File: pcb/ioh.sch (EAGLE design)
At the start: 11 parts, among them Q1 MOSFET-NCHANNEL2N7000

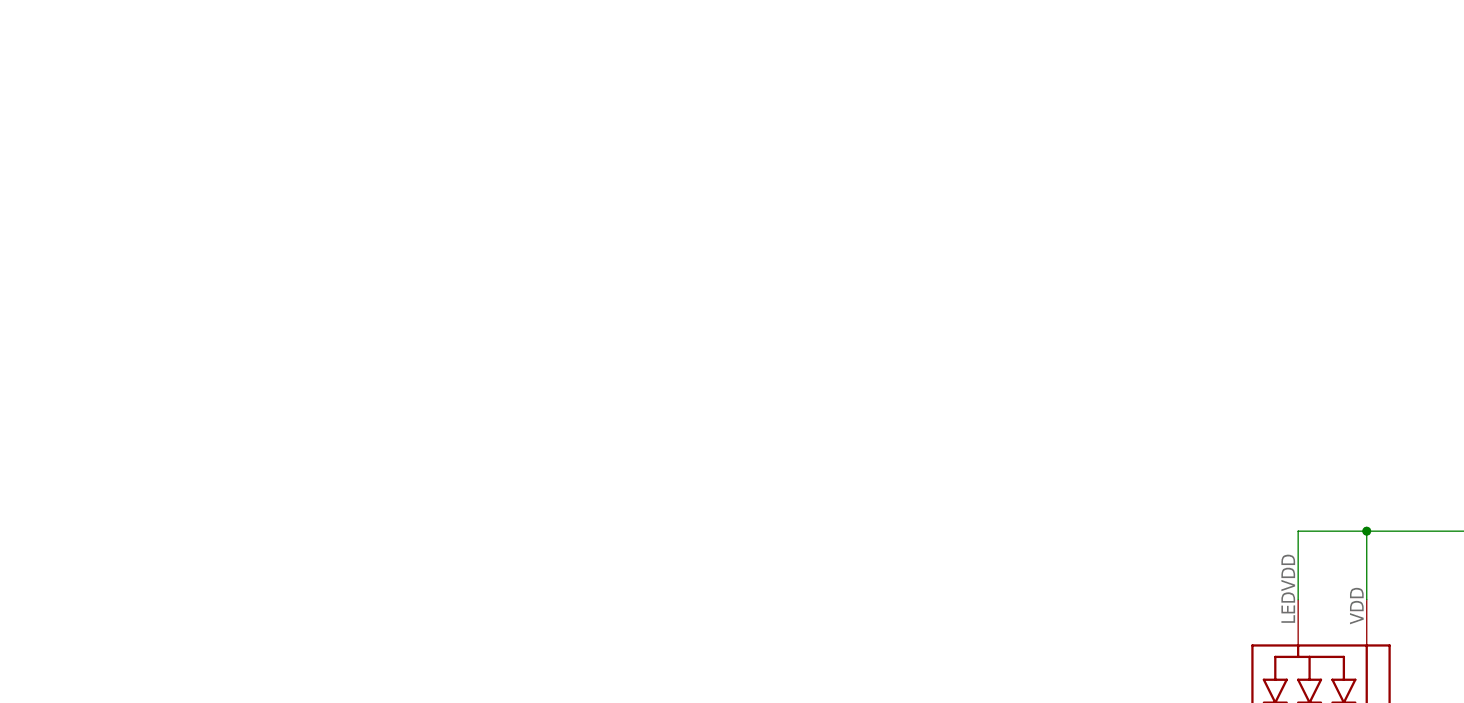
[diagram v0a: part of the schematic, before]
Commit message: add front/back tx
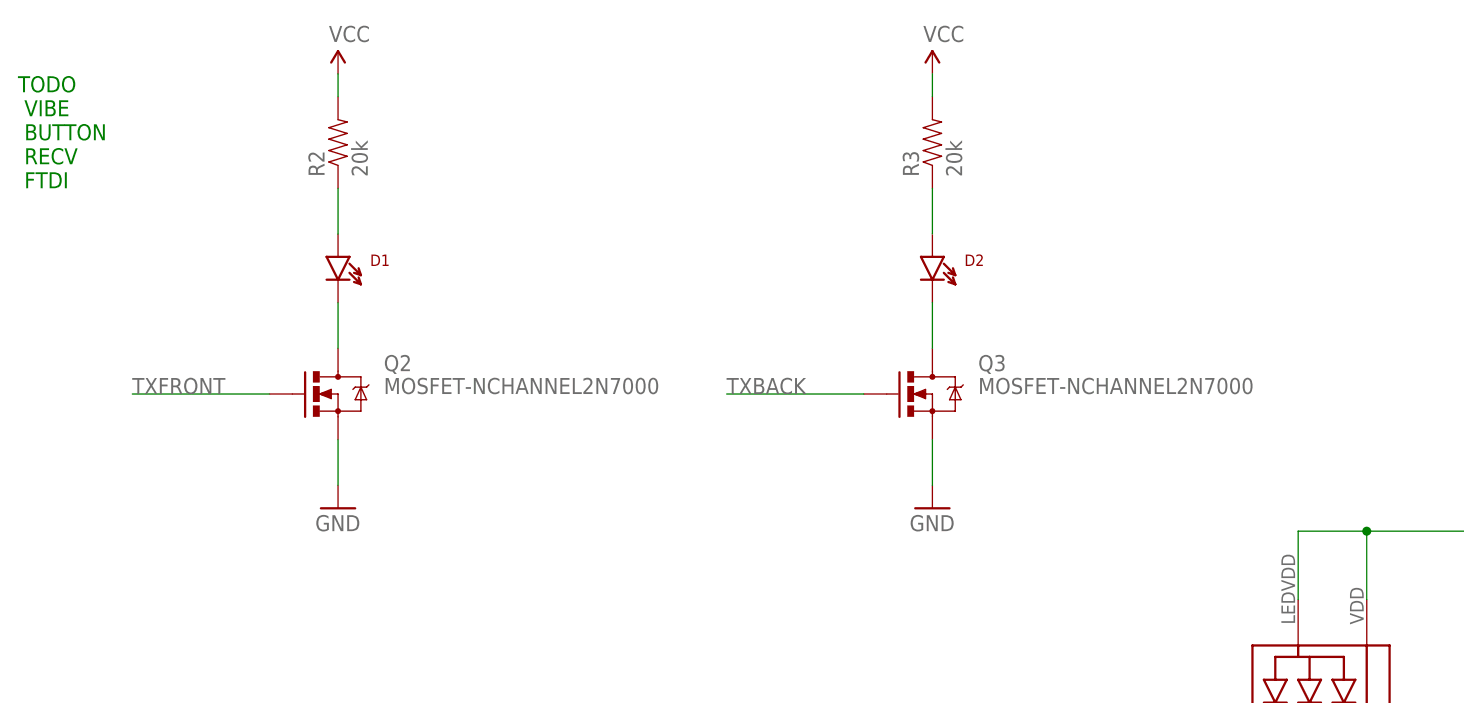
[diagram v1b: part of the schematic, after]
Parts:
- added D1, D2: (no value), SparkFun-LED:LTE-302
- added Q2, Q3: MOSFET-NCHANNEL2N7000, SparkFun-DiscreteSemi:MOSFET-NCHANNEL2N7000
- added R2, R3: 20k, SparkFun-Resistors:RESISTORPTH-1/4W
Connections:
- new net N$11: D1.C, Q2.D
- new net N$24: D2.A, R3.1
- new net N$25: D2.C, Q3.D
- new net N$4: D1.A, R2.1
- new net TXBACK: Q3.G
- new net TXFRONT: Q2.G
- net GND: now also Q2.S, Q3.S
- net VCC: now also R2.2, R3.2
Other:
- note added: "TODO VIBE BUTTON RECV FTDI"
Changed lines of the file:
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@@
 <part name="SUPPLY5" library="SparkFun-Aesthetics" deviceset="VCC" device=""/>
 <part name="R1" library="SparkFun-Resistors" deviceset="RESISTOR" device="PTH-1/4W" value="20k"/>
+<part name="D1" library="SparkFun-LED" deviceset="LTE-302" device=""/>
+<part name="SUPPLY6" library="SparkFun-Aesthetics" deviceset="VCC" device=""/>
+<part name="R2" library="SparkFun-Resistors" deviceset="RESISTOR" device="PTH-1/4W" value="20k"/>
+<part name="Q2" library="SparkFun-DiscreteSemi" deviceset="MOSFET-NCHANNEL" device="2N7000"/>
+<part name="GND5" library="SparkFun-Aesthetics" deviceset="GND" device=""/>
+<part name="D2" library="SparkFun-LED" deviceset="LTE-302" device=""/>
+<part name="SUPPLY7" library="SparkFun-Aesthetics" deviceset="VCC" device=""/>
+<part name="R3" library="SparkFun-Resistors" deviceset="RESISTOR" device="PTH-1/4W" value="20k"/>
+<part name="Q3" library="SparkFun-DiscreteSemi" deviceset="MOSFET-NCHANNEL" device="2N7000"/>
+<part name="GND6" library="SparkFun-Aesthetics" deviceset="GND" device=""/>
 </parts>
 <sheets>
 <sheet>
 <plain>
+<text x="-132.08" y="180.34" size="1.778" layer="91">TODO
+ VIBE
+ BUTTON
+ RECV
+ FTDI</text>
 </plain>
 <instances>
@@
 <instance part="SUPPLY5" gate="G$1" x="-38.1" y="106.68"/>
 <instance part="R1" gate="G$1" x="-38.1" y="99.06" rot="R90"/>
+<instance part="D1" gate="G$1" x="-96.52" y="172.72"/>
+<instance part="SUPPLY6" gate="G$1" x="-96.52" y="193.04"/>
+<instance part="R2" gate="G$1" x="-96.52" y="185.42" rot="R90"/>
+<instance part="Q2" gate="G$1" x="-96.52" y="157.48"/>
+<instance part="GND5" gate="1" x="-96.52" y="144.78"/>
+<instance part="D2" gate="G$1" x="-30.48" y="172.72"/>
+<instance part="SUPPLY7" gate="G$1" x="-30.48" y="193.04"/>
+<instance part="R3" gate="G$1" x="-30.48" y="185.42" rot="R90"/>
+<instance part="Q3" gate="G$1" x="-30.48" y="157.48"/>
+<instance part="GND6" gate="1" x="-30.48" y="144.78"/>
 </instances>
 <busses>
@@
 <pinref part="GND4" gate="1" pin="GND"/>
 <wire x1="-38.1" y1="76.2" x2="-38.1" y2="71.12" width="0.1524" layer="91"/>
+</segment>
+<segment>
+<pinref part="Q2" gate="G$1" pin="S"/>
+<pinref part="GND5" gate="1" pin="GND"/>
+<wire x1="-96.52" y1="152.4" x2="-96.52" y2="147.32" width="0.1524" layer="91"/>
+</segment>
+<segment>
+<pinref part="Q3" gate="G$1" pin="S"/>
+<pinref part="GND6" gate="1" pin="GND"/>
+<wire x1="-30.48" y1="152.4" x2="-30.48" y2="147.32" width="0.1524" layer="91"/>
 </segment>
 </net>
@@
 <wire x1="-38.1" y1="106.68" x2="-38.1" y2="104.14" width="0.1524" layer="91"/>
 </segment>
+<segment>
+<pinref part="SUPPLY6" gate="G$1" pin="VCC"/>
+<pinref part="R2" gate="G$1" pin="2"/>
+<wire x1="-96.52" y1="193.04" x2="-96.52" y2="190.5" width="0.1524" layer="91"/>
+</segment>
+<segment>
+<pinref part="SUPPLY7" gate="G$1" pin="VCC"/>
+<pinref part="R3" gate="G$1" pin="2"/>
+<wire x1="-30.48" y1="193.04" x2="-30.48" y2="190.5" width="0.1524" layer="91"/>
+</segment>
 </net>
 <net name="N$1" class="0">
@@
 </segment>
 </net>
+<net name="N$4" class="0">
+<segment>
+<pinref part="R2" gate="G$1" pin="1"/>
+<pinref part="D1" gate="G$1" pin="A"/>
+<wire x1="-96.52" y1="180.34" x2="-96.52" y2="175.26" width="0.1524" layer="91"/>
+</segment>
+</net>
+<net name="N$11" class="0">
+<segment>
+<pinref part="D1" gate="G$1" pin="C"/>
+<pinref part="Q2" gate="G$1" pin="D"/>
+<wire x1="-96.52" y1="167.64" x2="-96.52" y2="162.56" width="0.1524" layer="91"/>
+</segment>
+</net>
+<net name="TXBACK" class="0">
+<segment>
+<pinref part="Q3" gate="G$1" pin="G"/>
+<wire x1="-38.1" y1="157.48" x2="-53.34" y2="157.48" width="0.1524" layer="91"/>
+<label x="-53.34" y="157.48" size="1.778" layer="95"/>
+</segment>
+</net>
+<net name="N$24" class="0">
+<segment>
+<pinref part="R3" gate="G$1" pin="1"/>
+<pinref part="D2" gate="G$1" pin="A"/>
+<wire x1="-30.48" y1="180.34" x2="-30.48" y2="175.26" width="0.1524" layer="91"/>
+</segment>
+</net>
+<net name="N$25" class="0">
+<segment>
+<pinref part="D2" gate="G$1" pin="C"/>
+<pinref part="Q3" gate="G$1" pin="D"/>
+<wire x1="-30.48" y1="167.64" x2="-30.48" y2="162.56" width="0.1524" layer="91"/>
+</segment>
+</net>
+<net name="TXFRONT" class="0">
+<segment>
+<pinref part="Q2" gate="G$1" pin="G"/>
+<wire x1="-104.14" y1="157.48" x2="-119.38" y2="157.48" width="0.1524" layer="91"/>
+<label x="-119.38" y="157.48" size="1.778" layer="95"/>
+</segment>
+</net>
 </nets>
 </sheet>
@@
 </schematic>
 </drawing>
+<compatibility>
+<note version="6.3" minversion="6.2.2" severity="warning">
+Since Version 6.2.2 text objects can contain more than one line,
+which will not be processed correctly with this version.
+</note>
+</compatibility>
 </eagle>

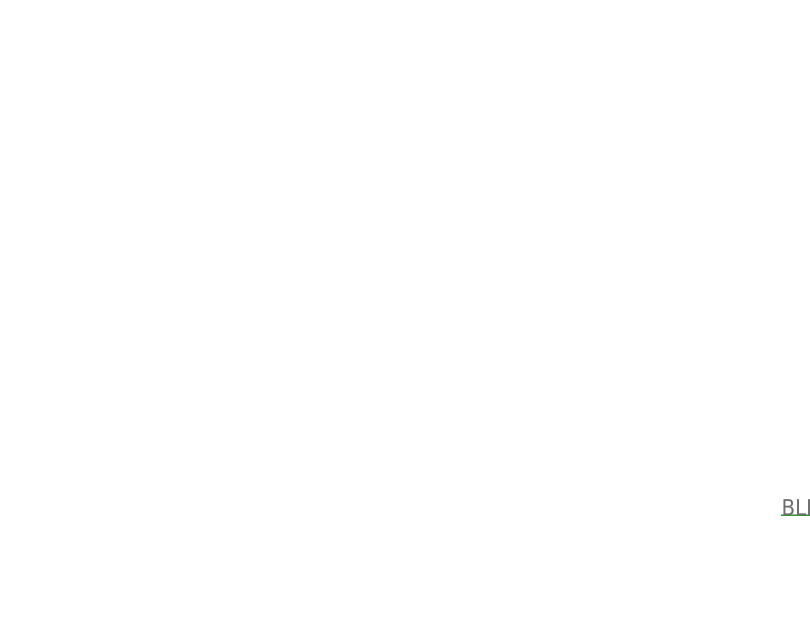
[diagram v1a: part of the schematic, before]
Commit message: tsop library addition; placement
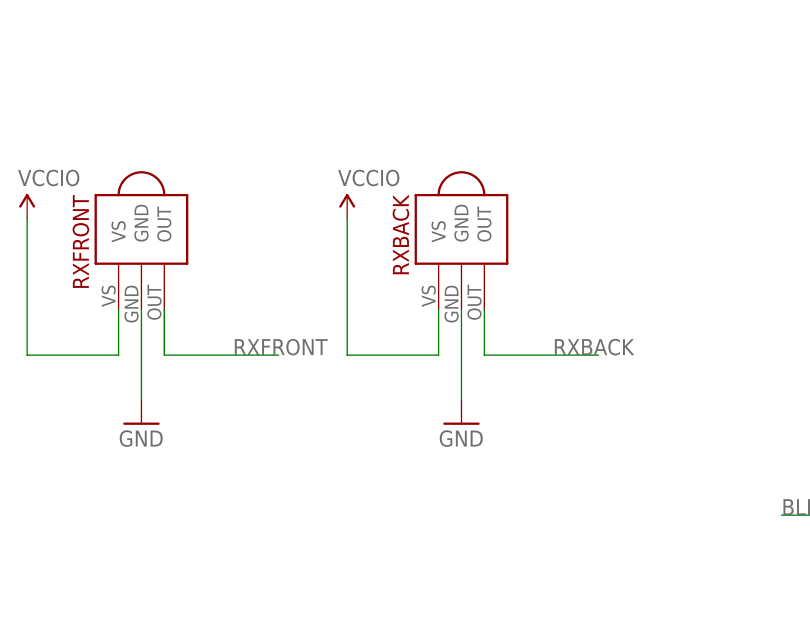
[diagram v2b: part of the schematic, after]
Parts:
- added RXBACK, RXFRONT: TSOP2438, ioh-1:TSOP2438
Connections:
- new net RXBACK: RXBACK.OUT
- new net RXFRONT: RXFRONT.OUT
- net GND: now also RXBACK.GND, RXFRONT.GND
- net VCCIO: now also RXBACK.VS, RXFRONT.VS
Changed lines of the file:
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@@
 <part name="Q3" library="SparkFun-DiscreteSemi" deviceset="MOSFET-NCHANNEL" device="2N7000"/>
 <part name="GND6" library="SparkFun-Aesthetics" deviceset="GND" device=""/>
+<part name="RXFRONT" library="ioh-1" deviceset="TSOP2438" device=""/>
+<part name="GND7" library="SparkFun-Aesthetics" deviceset="GND" device=""/>
+<part name="SUPPLY8" library="SparkFun-Aesthetics" deviceset="VCCIO" device=""/>
+<part name="RXBACK" library="ioh-1" deviceset="TSOP2438" device=""/>
+<part name="GND8" library="SparkFun-Aesthetics" deviceset="GND" device=""/>
+<part name="SUPPLY9" library="SparkFun-Aesthetics" deviceset="VCCIO" device=""/>
 </parts>
 <sheets>
@@
 <instance part="Q3" gate="G$1" x="-30.48" y="157.48"/>
 <instance part="GND6" gate="1" x="-30.48" y="144.78"/>
+<instance part="RXFRONT" gate="G$1" x="-121.92" y="116.84" rot="R270"/>
+<instance part="GND7" gate="1" x="-121.92" y="91.44"/>
+<instance part="SUPPLY8" gate="G$1" x="-134.62" y="114.3"/>
+<instance part="RXBACK" gate="G$1" x="-86.36" y="116.84" rot="R270"/>
+<instance part="GND8" gate="1" x="-86.36" y="91.44"/>
+<instance part="SUPPLY9" gate="G$1" x="-99.06" y="114.3"/>
 </instances>
 <busses>
@@
 <wire x1="-30.48" y1="152.4" x2="-30.48" y2="147.32" width="0.1524" layer="91"/>
 </segment>
+<segment>
+<pinref part="RXFRONT" gate="G$1" pin="GND"/>
+<pinref part="GND7" gate="1" pin="GND"/>
+<wire x1="-121.92" y1="104.14" x2="-121.92" y2="93.98" width="0.1524" layer="91"/>
+</segment>
+<segment>
+<pinref part="RXBACK" gate="G$1" pin="GND"/>
+<pinref part="GND8" gate="1" pin="GND"/>
+<wire x1="-86.36" y1="104.14" x2="-86.36" y2="93.98" width="0.1524" layer="91"/>
+</segment>
 </net>
 <net name="VCCIO" class="0">
@@
 <wire x1="22.86" y1="91.44" x2="22.86" y2="83.82" width="0.1524" layer="91"/>
 <junction x="22.86" y="83.82"/>
+</segment>
+<segment>
+<pinref part="SUPPLY8" gate="G$1" pin="VCCIO"/>
+<wire x1="-134.62" y1="114.3" x2="-134.62" y2="99.06" width="0.1524" layer="91"/>
+<wire x1="-134.62" y1="99.06" x2="-124.46" y2="99.06" width="0.1524" layer="91"/>
+<pinref part="RXFRONT" gate="G$1" pin="VS"/>
+<wire x1="-124.46" y1="99.06" x2="-124.46" y2="104.14" width="0.1524" layer="91"/>
+</segment>
+<segment>
+<pinref part="SUPPLY9" gate="G$1" pin="VCCIO"/>
+<wire x1="-99.06" y1="114.3" x2="-99.06" y2="99.06" width="0.1524" layer="91"/>
+<wire x1="-99.06" y1="99.06" x2="-88.9" y2="99.06" width="0.1524" layer="91"/>
+<pinref part="RXBACK" gate="G$1" pin="VS"/>
+<wire x1="-88.9" y1="99.06" x2="-88.9" y2="104.14" width="0.1524" layer="91"/>
 </segment>
 </net>
@@
 </segment>
 </net>
+<net name="RXFRONT" class="0">
+<segment>
+<pinref part="RXFRONT" gate="G$1" pin="OUT"/>
+<wire x1="-119.38" y1="104.14" x2="-119.38" y2="99.06" width="0.1524" layer="91"/>
+<wire x1="-119.38" y1="99.06" x2="-106.68" y2="99.06" width="0.1524" layer="91"/>
+<label x="-111.76" y="99.06" size="1.778" layer="95"/>
+</segment>
+</net>
+<net name="RXBACK" class="0">
+<segment>
+<pinref part="RXBACK" gate="G$1" pin="OUT"/>
+<wire x1="-83.82" y1="104.14" x2="-83.82" y2="99.06" width="0.1524" layer="91"/>
+<wire x1="-83.82" y1="99.06" x2="-71.12" y2="99.06" width="0.1524" layer="91"/>
+<label x="-76.2" y="99.06" size="1.778" layer="95"/>
+</segment>
+</net>

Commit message: vibe placement; update todo; caps
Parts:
- added C1: 10uF, SparkFun-Capacitors:10UF-25V-20%(PTH)KIT
- added JP3: M02PTH, SparkFun-Connectors:M02PTH
- added Q4: MOSFET-NCHANNEL2N7000, SparkFun-DiscreteSemi:MOSFET-NCHANNEL2N7000
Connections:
- new net N$13: JP3.2, Q4.D
- new net VIBE: Q4.G
- net GND: now also C1.-, Q4.S
- net VCC: now also JP3.1
- net VCCIO: now also C1.+
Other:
- note added: "TODO BUTTON FTDI"
- note removed: "TODO VIBE BUTTON RECV FTDI"
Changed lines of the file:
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@@
 <part name="GND8" library="SparkFun-Aesthetics" deviceset="GND" device=""/>
 <part name="SUPPLY9" library="SparkFun-Aesthetics" deviceset="VCCIO" device=""/>
+<part name="C1" library="SparkFun-Capacitors" deviceset="10UF-25V-20%(PTH)" device="KIT" value="10uF"/>
+<part name="JP3" library="SparkFun-Connectors" deviceset="M02" device="PTH"/>
+<part name="SUPPLY10" library="SparkFun-Aesthetics" deviceset="VCC" device=""/>
+<part name="GND9" library="SparkFun-Aesthetics" deviceset="GND" device=""/>
+<part name="Q4" library="SparkFun-DiscreteSemi" deviceset="MOSFET-NCHANNEL" device="2N7000"/>
 </parts>
 <sheets>
@@
 <plain>
 <text x="-132.08" y="180.34" size="1.778" layer="91">TODO
- VIBE
  BUTTON
- RECV
  FTDI</text>
 </plain>
@@
 <instance part="GND8" gate="1" x="-86.36" y="91.44"/>
 <instance part="SUPPLY9" gate="G$1" x="-99.06" y="114.3"/>
+<instance part="C1" gate="G$1" x="139.7" y="53.34"/>
+<instance part="JP3" gate="G$1" x="30.48" y="175.26" rot="R180"/>
+<instance part="SUPPLY10" gate="G$1" x="15.24" y="190.5"/>
+<instance part="GND9" gate="1" x="15.24" y="152.4"/>
+<instance part="Q4" gate="G$1" x="15.24" y="162.56"/>
 </instances>
 <busses>
@@
 <pinref part="GND1" gate="1" pin="GND"/>
 <wire x1="124.46" y1="48.26" x2="124.46" y2="45.72" width="0.1524" layer="91"/>
+<pinref part="C1" gate="G$1" pin="-"/>
+<wire x1="139.7" y1="48.26" x2="139.7" y2="45.72" width="0.1524" layer="91"/>
+<wire x1="139.7" y1="45.72" x2="124.46" y2="45.72" width="0.1524" layer="91"/>
+<junction x="124.46" y="45.72"/>
 </segment>
 <segment>
@@
 <wire x1="-86.36" y1="104.14" x2="-86.36" y2="93.98" width="0.1524" layer="91"/>
 </segment>
+<segment>
+<pinref part="GND9" gate="1" pin="GND"/>
+<pinref part="Q4" gate="G$1" pin="S"/>
+<wire x1="15.24" y1="154.94" x2="15.24" y2="157.48" width="0.1524" layer="91"/>
+</segment>
 </net>
 <net name="VCCIO" class="0">
@@
 <wire x1="104.14" y1="60.96" x2="124.46" y2="60.96" width="0.1524" layer="91"/>
 <junction x="124.46" y="60.96"/>
+<pinref part="C1" gate="G$1" pin="+"/>
+<wire x1="139.7" y1="55.88" x2="139.7" y2="60.96" width="0.1524" layer="91"/>
+<wire x1="139.7" y1="60.96" x2="124.46" y2="60.96" width="0.1524" layer="91"/>
 </segment>
 <segment>
@@
 <wire x1="-30.48" y1="193.04" x2="-30.48" y2="190.5" width="0.1524" layer="91"/>
 </segment>
+<segment>
+<pinref part="JP3" gate="G$1" pin="1"/>
+<wire x1="22.86" y1="175.26" x2="15.24" y2="175.26" width="0.1524" layer="91"/>
+<pinref part="SUPPLY10" gate="G$1" pin="VCC"/>
+<wire x1="15.24" y1="175.26" x2="15.24" y2="190.5" width="0.1524" layer="91"/>
+</segment>
 </net>
 <net name="N$1" class="0">
@@
 </segment>
 </net>
+<net name="N$13" class="0">
+<segment>
+<pinref part="Q4" gate="G$1" pin="D"/>
+<pinref part="JP3" gate="G$1" pin="2"/>
+<wire x1="15.24" y1="167.64" x2="15.24" y2="172.72" width="0.1524" layer="91"/>
+<wire x1="15.24" y1="172.72" x2="22.86" y2="172.72" width="0.1524" layer="91"/>
+</segment>
+</net>
+<net name="VIBE" class="0">
+<segment>
+<pinref part="Q4" gate="G$1" pin="G"/>
+<wire x1="7.62" y1="162.56" x2="-10.16" y2="162.56" width="0.1524" layer="91"/>
+<label x="-10.16" y="162.56" size="1.778" layer="95"/>
+</segment>
+</net>

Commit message: add switch
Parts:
- added S1: (no value), adafruit:40-XX
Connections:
- new net BOOP: S1.S, S1.S1
- net GND: now also S1.P, S1.P1
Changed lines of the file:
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@@
 <part name="GND9" library="SparkFun-Aesthetics" deviceset="GND" device=""/>
 <part name="Q4" library="SparkFun-DiscreteSemi" deviceset="MOSFET-NCHANNEL" device="2N7000"/>
+<part name="S1" library="adafruit" deviceset="40-XX" device=""/>
+<part name="GND10" library="SparkFun-Aesthetics" deviceset="GND" device=""/>
 </parts>
 <sheets>
@@
 <instance part="GND9" gate="1" x="15.24" y="152.4"/>
 <instance part="Q4" gate="G$1" x="15.24" y="162.56"/>
+<instance part="S1" gate="1" x="-114.3" y="63.5"/>
+<instance part="GND10" gate="1" x="-114.3" y="45.72"/>
 </instances>
 <busses>
@@
 <pinref part="Q4" gate="G$1" pin="S"/>
 <wire x1="15.24" y1="154.94" x2="15.24" y2="157.48" width="0.1524" layer="91"/>
+</segment>
+<segment>
+<pinref part="S1" gate="1" pin="P"/>
+<pinref part="GND10" gate="1" pin="GND"/>
+<wire x1="-114.3" y1="58.42" x2="-114.3" y2="55.88" width="0.1524" layer="91"/>
+<pinref part="S1" gate="1" pin="P1"/>
+<wire x1="-114.3" y1="55.88" x2="-114.3" y2="48.26" width="0.1524" layer="91"/>
+<wire x1="-111.76" y1="58.42" x2="-111.76" y2="55.88" width="0.1524" layer="91"/>
+<wire x1="-111.76" y1="55.88" x2="-114.3" y2="55.88" width="0.1524" layer="91"/>
+<junction x="-114.3" y="55.88"/>
 </segment>
 </net>
@@
 </segment>
 </net>
+<net name="BOOP" class="0">
+<segment>
+<pinref part="S1" gate="1" pin="S"/>
+<wire x1="-114.3" y1="68.58" x2="-114.3" y2="71.12" width="0.1524" layer="91"/>
+<pinref part="S1" gate="1" pin="S1"/>
+<wire x1="-111.76" y1="68.58" x2="-111.76" y2="71.12" width="0.1524" layer="91"/>
+<wire x1="-111.76" y1="71.12" x2="-114.3" y2="71.12" width="0.1524" layer="91"/>
+<junction x="-114.3" y="71.12"/>
+<wire x1="-114.3" y1="71.12" x2="-88.9" y2="71.12" width="0.1524" layer="91"/>
+<label x="-96.52" y="71.12" size="1.778" layer="95"/>
+</segment>
+</net>
